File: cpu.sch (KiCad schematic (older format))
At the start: 9 parts, among them IC1 STM32L051K8T6, SW1 SW_PUSH

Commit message: Increase clearance for fill zones to 0.4mm
Signed-off-by: Philip Luyckx <philip.luyckx@gmail.com>
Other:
- note added: "Peripherals:\nRF module (SPI, CSN, CE, IRQ)\nDHT (1wire, enable)\nLight sensor (adc, enable)\nMotion (ADC, enable)\nUART\nSWD"
- note removed: "Peripherals:\nRF module (SPI, CSN, CE, IRQ)\nDHT (1wire, enable)\nLight sensor (adc, enable)\nMotion (ADC, enable)\nUART\nSWD\nRelay"
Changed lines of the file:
@@
 NoConn ~ 7050 3200
 Text Notes 7850 2650 0    60   ~ 0
-Peripherals:\nRF module (SPI, CSN, CE, IRQ)\nDHT (1wire, enable)\nLight sensor (adc, enable)\nMotion (ADC, enable)\nUART\nSWD\nRelay
+Peripherals:\nRF module (SPI, CSN, CE, IRQ)\nDHT (1wire, enable)\nLight sensor (adc, enable)\nMotion (ADC, enable)\nUART\nSWD
 Text GLabel 5350 3900 0    60   Output ~ 0
 MCU_LED

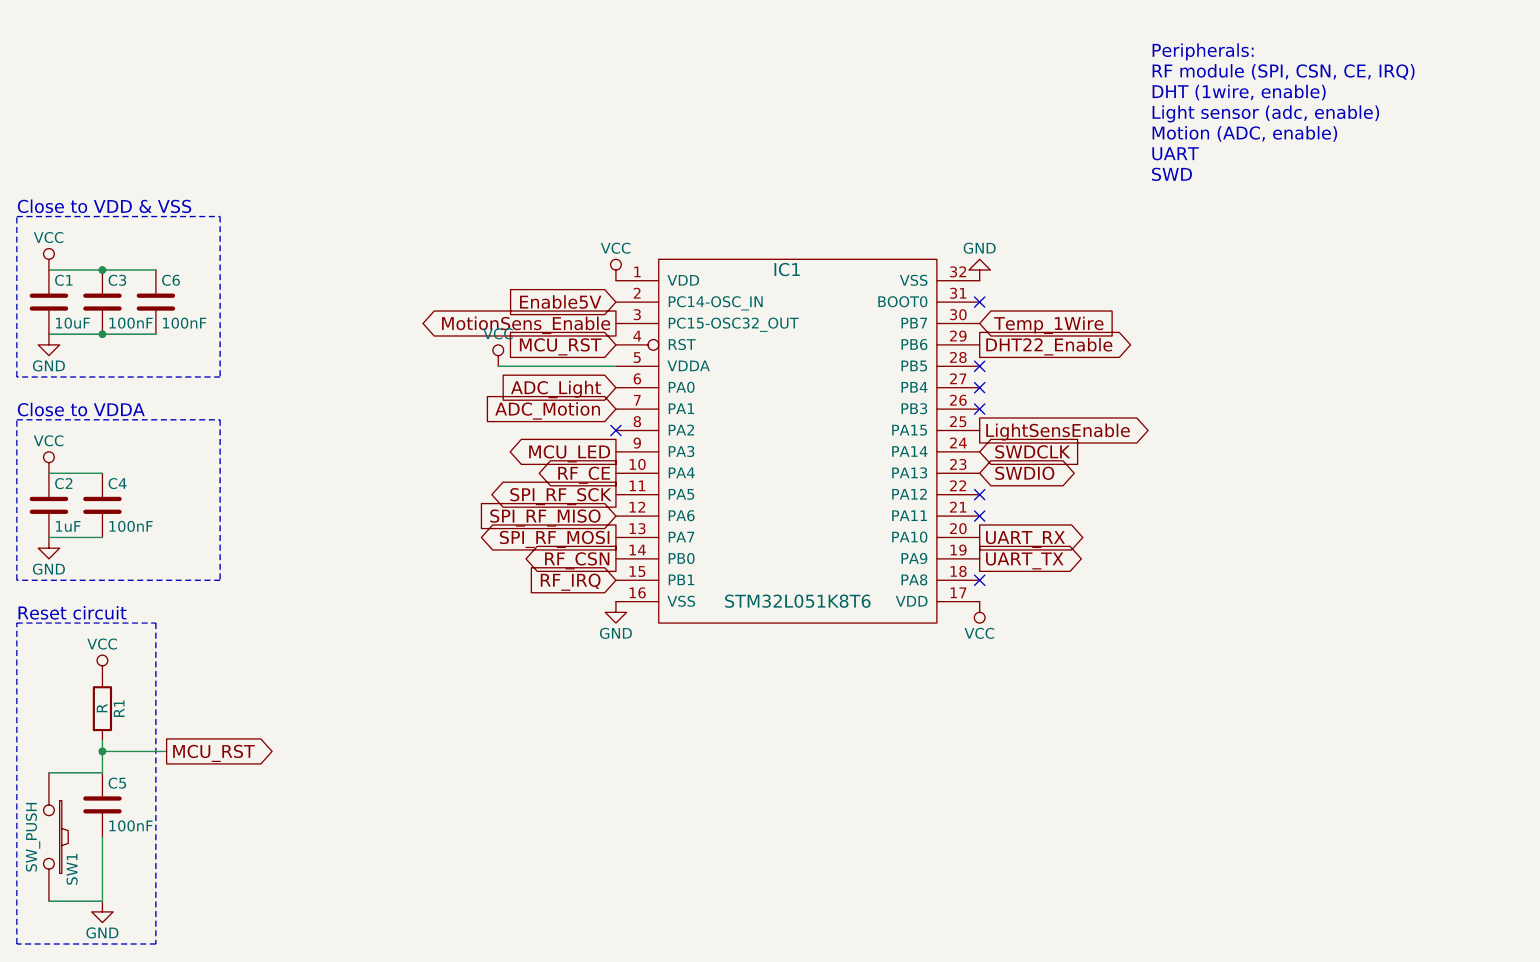
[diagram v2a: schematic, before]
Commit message: Update schematic and reroute print
 * Update opamp circuit for light sensor
 * Change opamp
 * Reroute everything

Signed-off-by: Philip Luyckx <philip.luyckx@gmail.com>
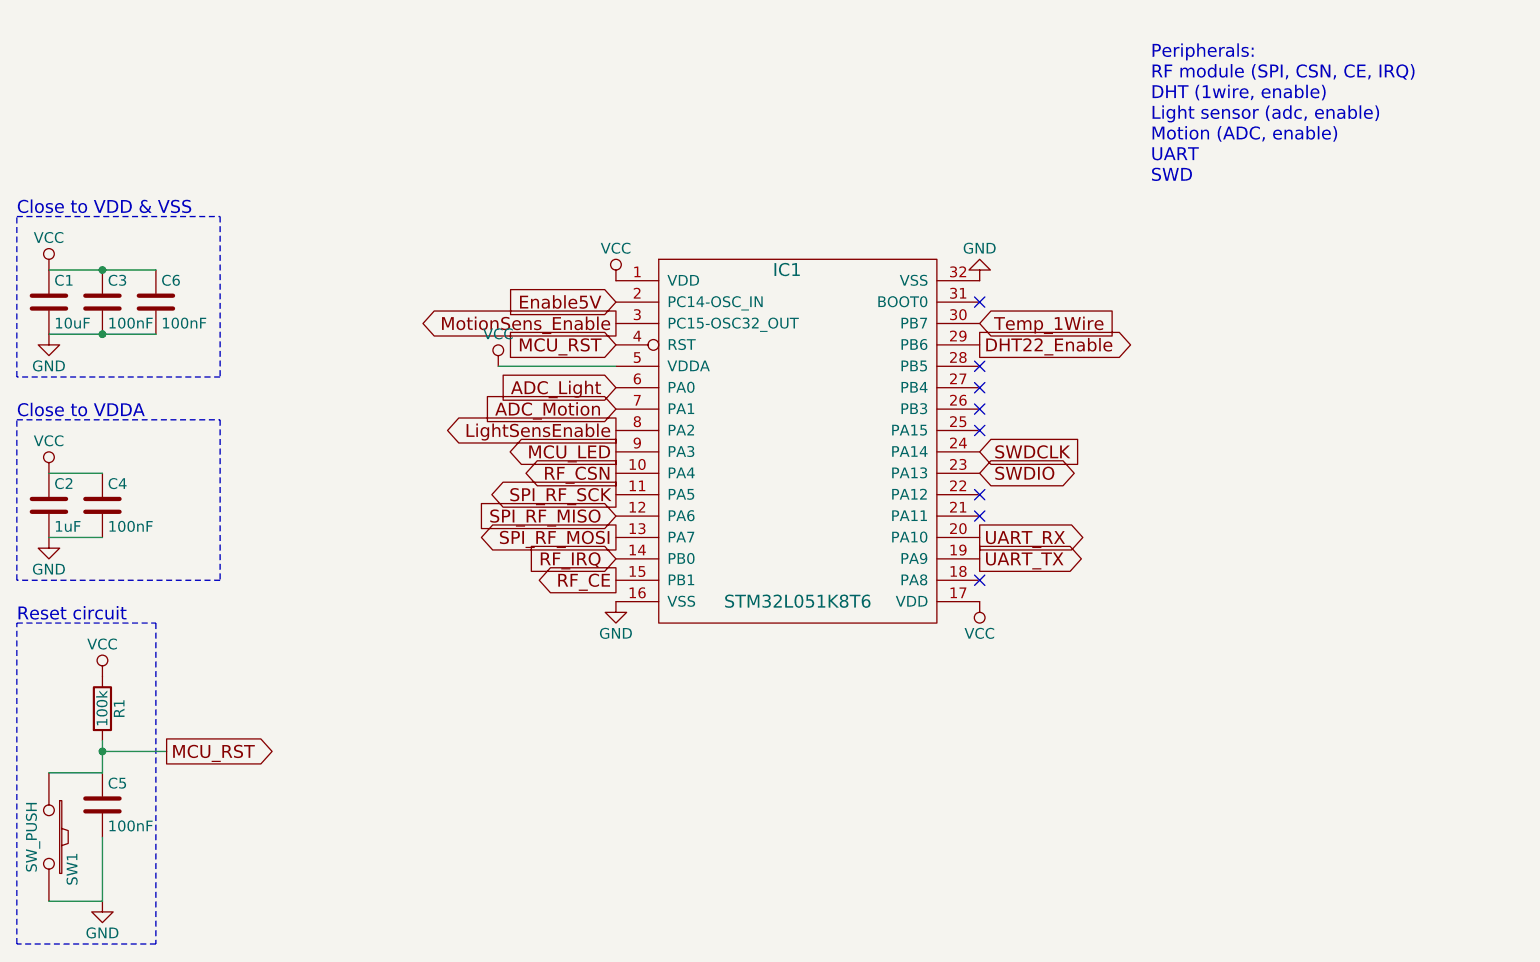
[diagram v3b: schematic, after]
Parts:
- R1: value R -> 100k
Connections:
- net LightSensEnable: now also IC1.8 (PA2); no longer IC1.25 (PA15)
- net RF_CE: now also IC1.15 (PB1); no longer IC1.10 (PA4)
- net RF_CSN: now also IC1.10 (PA4); no longer IC1.14 (PB0)
- net RF_IRQ: now also IC1.14 (PB0); no longer IC1.15 (PB1)
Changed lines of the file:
@@
 $EndDescr
 $Comp
-L VCC #PWR1
+L VCC #PWR01
 U 1 1 565E0F45
 P 2700 3050
-F 0 "#PWR1" H 2700 2900 50  0001 C CNN
+F 0 "#PWR01" H 2700 2900 50  0001 C CNN
 F 1 "VCC" H 2700 3200 50  0000 C CNN
 F 2 "" H 2700 3050 60  0000 C CNN
@@
 $EndComp
 $Comp
-L GND #PWR2
+L GND #PWR02
 U 1 1 565E0F59
 P 2700 3350
-F 0 "#PWR2" H 2700 3100 50  0001 C CNN
+F 0 "#PWR02" H 2700 3100 50  0001 C CNN
 F 1 "GND" H 2700 3200 50  0000 C CNN
 F 2 "" H 2700 3350 60  0000 C CNN
@@
 Connection ~ 2950 3350
 $Comp
-L VCC #PWR8
+L VCC #PWR03
 U 1 1 565E1082
 P 5350 3100
-F 0 "#PWR8" H 5350 2950 50  0001 C CNN
+F 0 "#PWR03" H 5350 2950 50  0001 C CNN
 F 1 "VCC" H 5350 3250 50  0000 C CNN
 F 2 "" H 5350 3100 60  0000 C CNN
@@
 $EndComp
 $Comp
-L VCC #PWR11
+L VCC #PWR04
 U 1 1 565E109E
 P 7050 4600
-F 0 "#PWR11" H 7050 4450 50  0001 C CNN
+F 0 "#PWR04" H 7050 4450 50  0001 C CNN
 F 1 "VCC" H 7050 4750 50  0000 C CNN
 F 2 "" H 7050 4600 60  0000 C CNN
@@
 $EndComp
 $Comp
-L GND #PWR10
+L GND #PWR05
 U 1 1 565E10BA
 P 7050 3100
-F 0 "#PWR10" H 7050 2850 50  0001 C CNN
+F 0 "#PWR05" H 7050 2850 50  0001 C CNN
 F 1 "GND" H 7050 2950 50  0000 C CNN
 F 2 "" H 7050 3100 60  0000 C CNN
@@
 $EndComp
 $Comp
-L GND #PWR9
+L GND #PWR06
 U 1 1 565E10D6
 P 5350 4600
-F 0 "#PWR9" H 5350 4350 50  0001 C CNN
+F 0 "#PWR06" H 5350 4350 50  0001 C CNN
 F 1 "GND" H 5350 4450 50  0000 C CNN
 F 2 "" H 5350 4600 60  0000 C CNN
@@
 $EndComp
 $Comp
-L VCC #PWR3
+L VCC #PWR07
 U 1 1 565E12D0
 P 2700 4000
-F 0 "#PWR3" H 2700 3850 50  0001 C CNN
+F 0 "#PWR07" H 2700 3850 50  0001 C CNN
 F 1 "VCC" H 2700 4150 50  0000 C CNN
 F 2 "" H 2700 4000 60  0000 C CNN
@@
 $EndComp
 $Comp
-L GND #PWR4
+L GND #PWR08
 U 1 1 565E12F0
 P 2700 4300
-F 0 "#PWR4" H 2700 4050 50  0001 C CNN
+F 0 "#PWR08" H 2700 4050 50  0001 C CNN
 F 1 "GND" H 2700 4150 50  0000 C CNN
 F 2 "" H 2700 4300 60  0000 C CNN
@@
 P 2950 5100
 F 0 "R1" V 3030 5100 50  0000 C CNN
-F 1 "R" V 2950 5100 50  0000 C CNN
+F 1 "100k" V 2950 5100 50  0000 C CNN
 F 2 "Resistors_SMD:R_1206" V 2880 5100 30  0001 C CNN
 F 3 "" H 2950 5100 30  0000 C CNN
@@
 $EndComp
 $Comp
-L VCC #PWR5
+L VCC #PWR09
 U 1 1 565E15CE
 P 2950 4950
-F 0 "#PWR5" H 2950 4800 50  0001 C CNN
+F 0 "#PWR09" H 2950 4800 50  0001 C CNN
 F 1 "VCC" H 2950 5100 50  0000 C CNN
 F 2 "" H 2950 4950 60  0000 C CNN
@@
 $EndComp
 $Comp
-L GND #PWR6
+L GND #PWR010
 U 1 1 565E15F4
 P 2950 6000
-F 0 "#PWR6" H 2950 5750 50  0001 C CNN
+F 0 "#PWR010" H 2950 5750 50  0001 C CNN
 F 1 "GND" H 2950 5850 50  0000 C CNN
 F 2 "" H 2950 6000 60  0000 C CNN
@@
 MCU_RST
 $Comp
-L VCC #PWR7
+L VCC #PWR011
 U 1 1 565E178E
 P 4800 3500
-F 0 "#PWR7" H 4800 3350 50  0001 C CNN
+F 0 "#PWR011" H 4800 3350 50  0001 C CNN
 F 1 "VCC" H 4800 3650 50  0000 C CNN
 F 2 "" H 4800 3500 60  0000 C CNN
@@
 Text GLabel 7050 4300 2    60   Output ~ 0
 UART_RX
-Text GLabel 7050 3800 2    60   Output ~ 0
+Text GLabel 5350 3800 0    60   Output ~ 0
 LightSensEnable
 Text GLabel 7050 4000 2    60   BiDi ~ 0
@@
 Text GLabel 7050 3900 2    60   Input ~ 0
 SWDCLK
-Text GLabel 5350 4400 0    60   Output ~ 0
+Text GLabel 5350 4000 0    60   Output ~ 0
 RF_CSN
-Text GLabel 5350 4000 0    60   Output ~ 0
+Text GLabel 5350 4500 0    60   Output ~ 0
 RF_CE
-Text GLabel 5350 4500 0    60   Input ~ 0
+Text GLabel 5350 4400 0    60   Input ~ 0
 RF_IRQ
 NoConn ~ 7050 3200
@@
 NoConn ~ 7050 3600
 NoConn ~ 7050 3500
-NoConn ~ 5350 3800
+NoConn ~ 7050 3800
 NoConn ~ 7050 4200
 NoConn ~ 7050 4100

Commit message: Use 0603 resistors
Signed-off-by: Philip Luyckx <philip.luyckx@gmail.com>
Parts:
- R1: footprint Resistors_SMD:R_1206 -> Resistors_SMD:R_0603
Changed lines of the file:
@@
 F 0 "R1" V 3030 5100 50  0000 C CNN
 F 1 "100k" V 2950 5100 50  0000 C CNN
-F 2 "Resistors_SMD:R_1206" V 2880 5100 30  0001 C CNN
+F 2 "Resistors_SMD:R_0603" V 2880 5100 30  0001 C CNN
 F 3 "" H 2950 5100 30  0000 C CNN
 	1    2950 5100

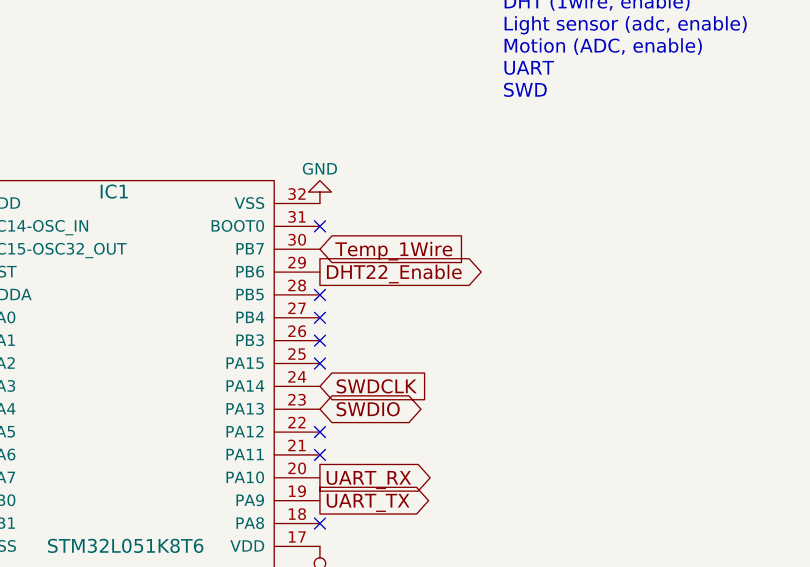
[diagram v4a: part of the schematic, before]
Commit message: Update pull-up resistor for a sensor
Signed-off-by: Philip Luyckx <philip.luyckx@gmail.com>
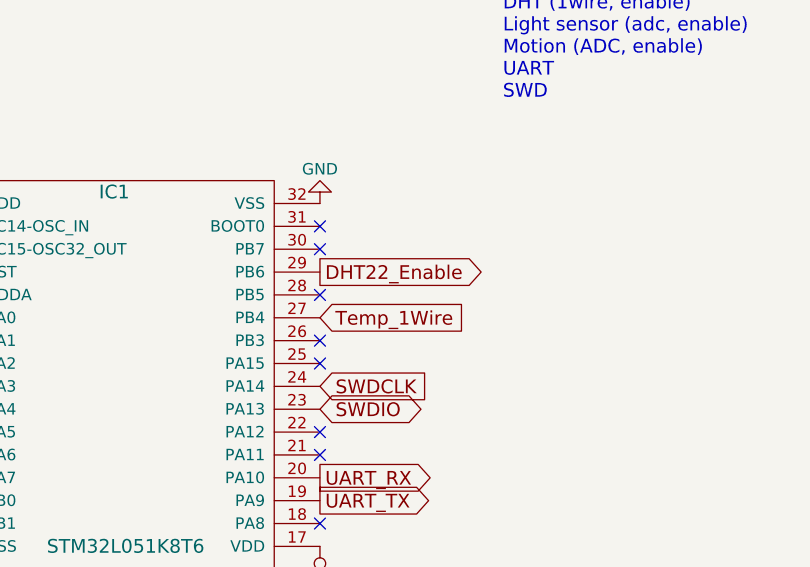
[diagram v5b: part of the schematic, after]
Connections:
- net Temp_1Wire: now also IC1.27 (PB4); no longer IC1.30 (PB7)
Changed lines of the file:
@@
 Text GLabel 5350 3700 0    60   Input ~ 0
 ADC_Motion
-Text GLabel 7050 3300 2    60   Input ~ 0
+Text GLabel 7050 3600 2    60   Input ~ 0
 Temp_1Wire
 Text GLabel 7050 3400 2    60   Output ~ 0
@@
 Text GLabel 5350 3900 0    60   Output ~ 0
 MCU_LED
-NoConn ~ 7050 3600
+NoConn ~ 7050 3300
 NoConn ~ 7050 3500
 NoConn ~ 7050 3800

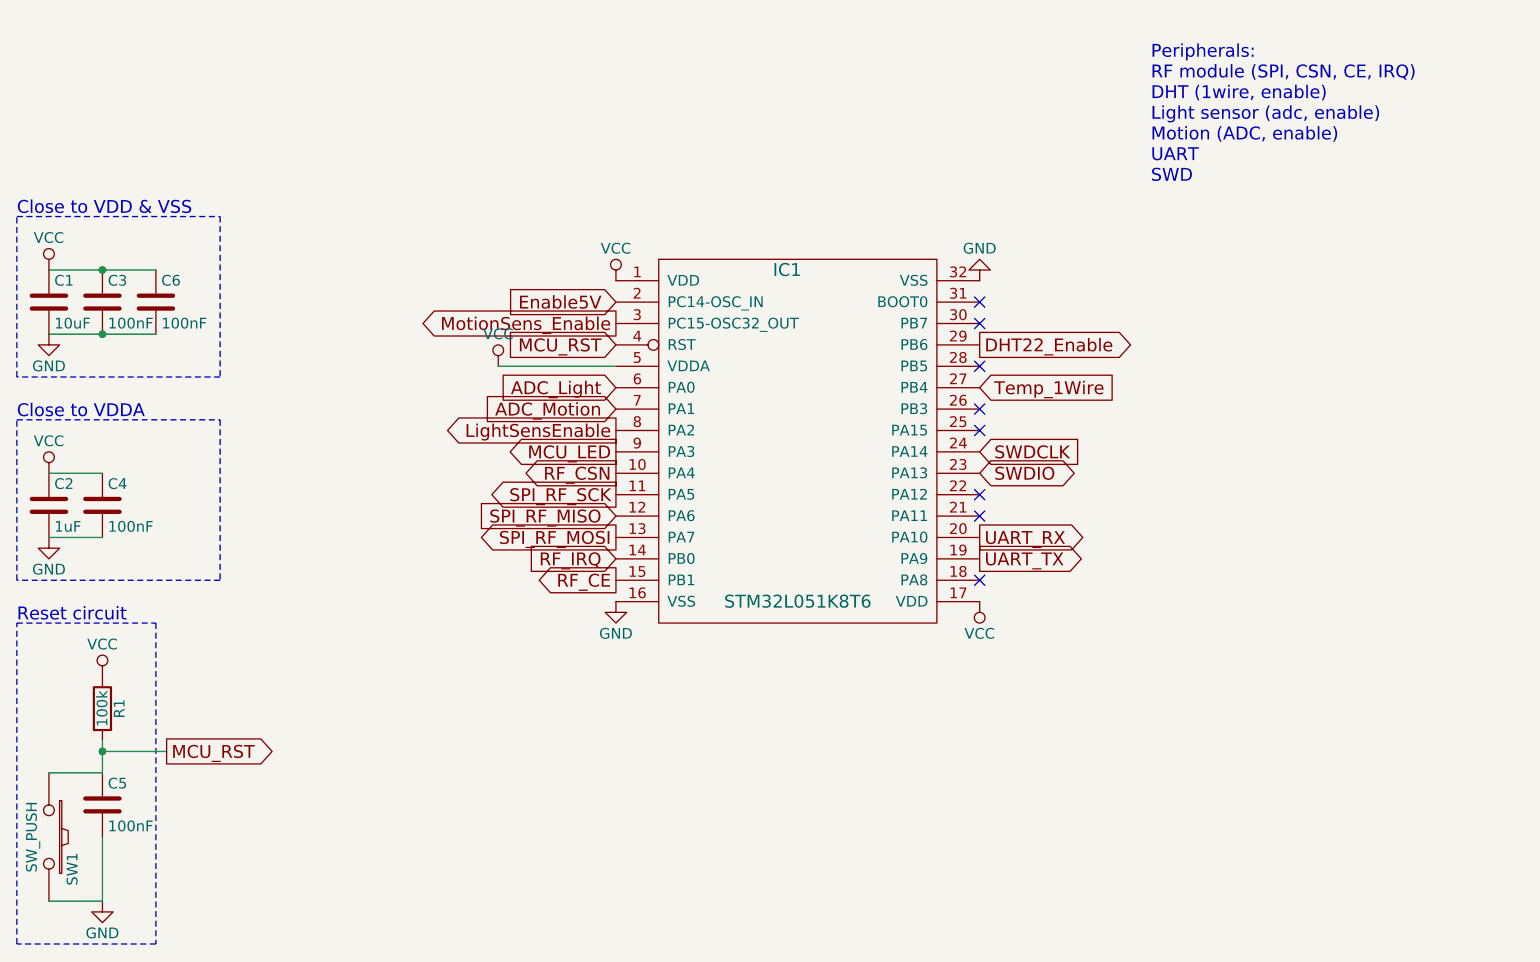
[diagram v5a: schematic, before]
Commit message: Finish work on V2
 * Rework layout
 * Reassign mcu pins
 * Add a capacitor for the RF module

Signed-off-by: Philip Luyckx <philip.luyckx@gmail.com>
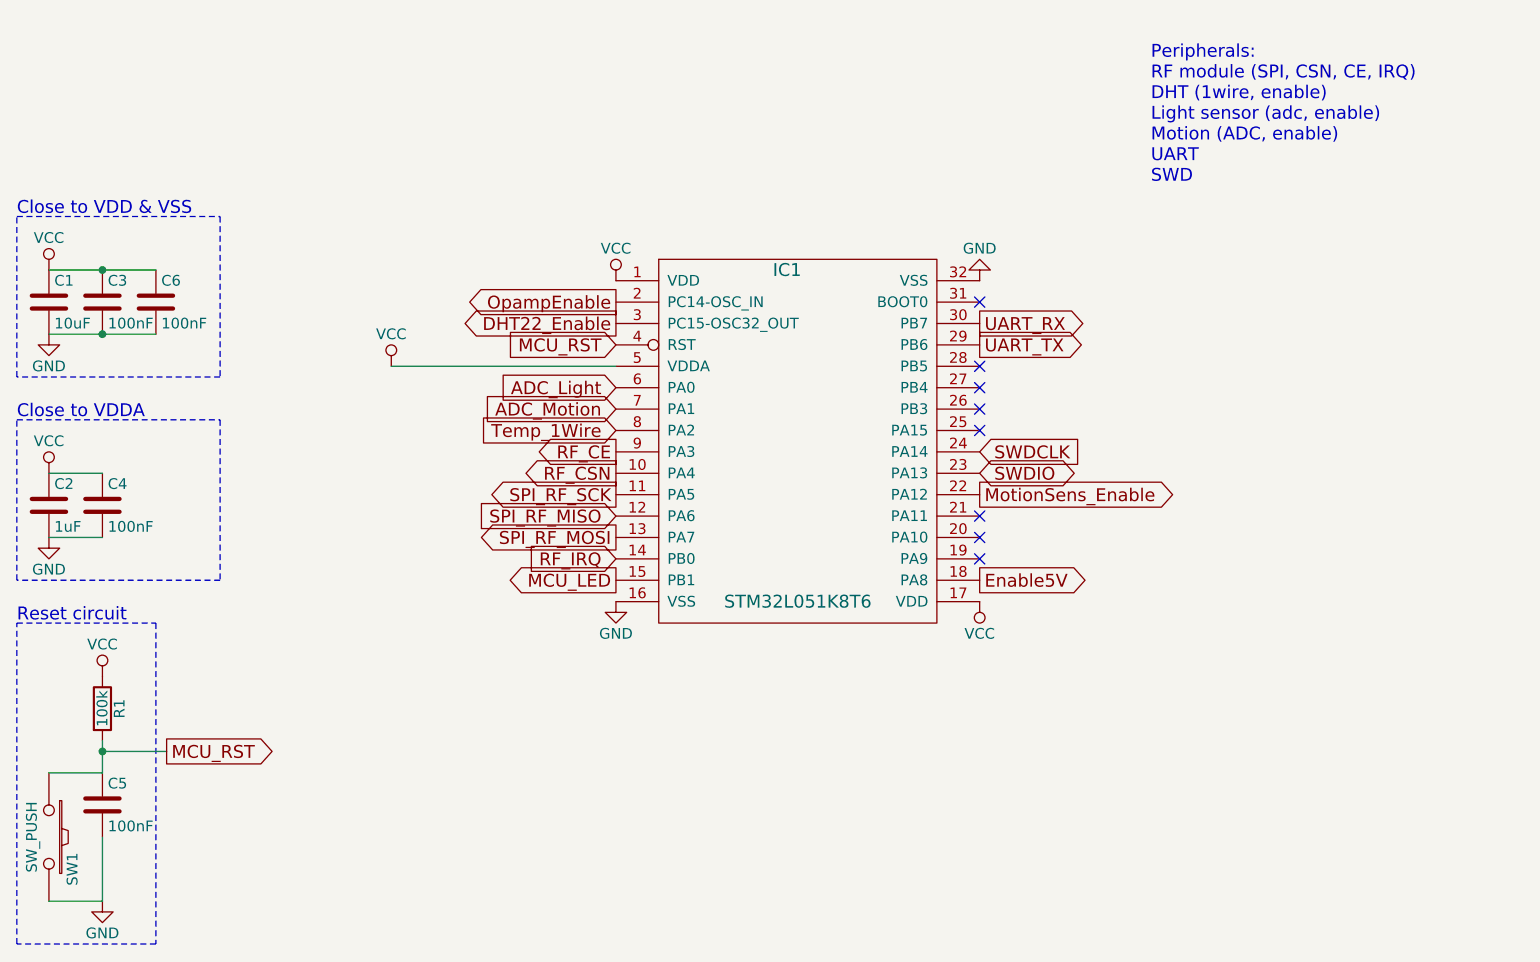
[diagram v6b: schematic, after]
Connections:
- net LightSensEnable is gone; now on net Temp_1Wire: IC1.8 (PA2)
- net DHT22_Enable: now also IC1.3 (PC15-OSC32_OUT); no longer IC1.29 (PB6)
- net Enable5V: now also IC1.18 (PA8); no longer IC1.2 (PC14-OSC_IN)
- net MCU_LED: now also IC1.15 (PB1); no longer IC1.9 (PA3)
- net MotionSens_Enable: now also IC1.22 (PA12); no longer IC1.3 (PC15-OSC32_OUT)
- net RF_CE: now also IC1.9 (PA3); no longer IC1.15 (PB1)
- net Temp_1Wire: no longer IC1.27 (PB4)
- net UART_RX: now also IC1.30 (PB7); no longer IC1.20 (PA10)
- net UART_TX: now also IC1.29 (PB6); no longer IC1.19 (PA9)
- new net OpampEnable: IC1.2 (PC14-OSC_IN)
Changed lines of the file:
@@
 L VCC #PWR011
 U 1 1 565E178E
-P 4800 3500
-F 0 "#PWR011" H 4800 3350 50  0001 C CNN
-F 1 "VCC" H 4800 3650 50  0000 C CNN
-F 2 "" H 4800 3500 60  0000 C CNN
-F 3 "" H 4800 3500 60  0000 C CNN
-	1    4800 3500
+P 4300 3500
+F 0 "#PWR011" H 4300 3350 50  0001 C CNN
+F 1 "VCC" H 4300 3650 50  0000 C CNN
+F 2 "" H 4300 3500 60  0000 C CNN
+F 3 "" H 4300 3500 60  0000 C CNN
+	1    4300 3500
 	1    0    0    -1
 $EndComp
 Wire Wire Line
-	4800 3500 5350 3500
+	4300 3500 5350 3500
 Wire Notes Line
 	2550 4700 3200 4700
@@
 Text GLabel 5350 3700 0    60   Input ~ 0
 ADC_Motion
-Text GLabel 7050 3600 2    60   Input ~ 0
+Text GLabel 5350 3800 0    60   Input ~ 0
 Temp_1Wire
-Text GLabel 7050 3400 2    60   Output ~ 0
+Text GLabel 5350 3300 0    60   Output ~ 0
 DHT22_Enable
 Text GLabel 5350 4100 0    60   Output ~ 0
@@
 Text GLabel 5350 4300 0    60   Output ~ 0
 SPI_RF_MOSI
-Text GLabel 5350 3300 0    60   Output ~ 0
+Text GLabel 7050 4100 2    60   Output ~ 0
 MotionSens_Enable
-Text GLabel 7050 4400 2    60   Output ~ 0
+Text GLabel 7050 3400 2    60   Output ~ 0
 UART_TX
-Text GLabel 7050 4300 2    60   Output ~ 0
+Text GLabel 7050 3300 2    60   Output ~ 0
 UART_RX
-Text GLabel 5350 3800 0    60   Output ~ 0
-LightSensEnable
+Text GLabel 5350 3200 0    60   Output ~ 0
+OpampEnable
 Text GLabel 7050 4000 2    60   BiDi ~ 0
 SWDIO
@@
 Text GLabel 5350 4000 0    60   Output ~ 0
 RF_CSN
-Text GLabel 5350 4500 0    60   Output ~ 0
+Text GLabel 5350 3900 0    60   Output ~ 0
 RF_CE
 Text GLabel 5350 4400 0    60   Input ~ 0
@@
 Text Notes 7850 2650 0    60   ~ 0
 Peripherals:\nRF module (SPI, CSN, CE, IRQ)\nDHT (1wire, enable)\nLight sensor (adc, enable)\nMotion (ADC, enable)\nUART\nSWD
-Text GLabel 5350 3900 0    60   Output ~ 0
+Text GLabel 5350 4500 0    60   Output ~ 0
 MCU_LED
-NoConn ~ 7050 3300
+NoConn ~ 7050 3800
 NoConn ~ 7050 3500
-NoConn ~ 7050 3800
+NoConn ~ 7050 3600
 NoConn ~ 7050 4200
-NoConn ~ 7050 4100
+NoConn ~ 7050 4300
 NoConn ~ 7050 3700
 $Comp
@@
 	1    0    0    -1
 $EndComp
-NoConn ~ 7050 4500
-Text GLabel 5350 3200 0    60   Input ~ 0
+NoConn ~ 7050 4400
+Text GLabel 7050 4500 2    60   Output ~ 0
 Enable5V
 $EndSCHEMATC
